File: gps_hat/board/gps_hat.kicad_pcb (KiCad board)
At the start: 2 copper layers, 12 parts, among them IC1 MTK3339, J1 Conn_02x10_Odd_Even, J2 U.FL-R-SMT(10)

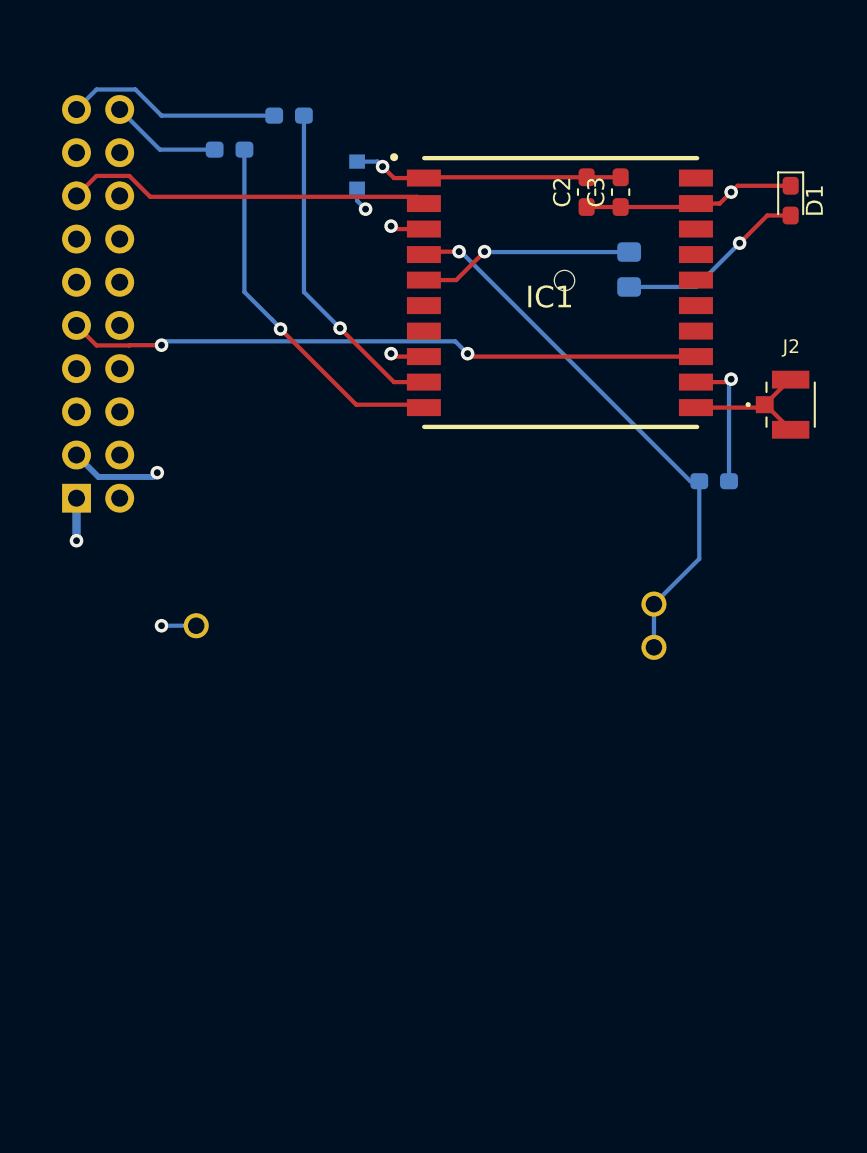
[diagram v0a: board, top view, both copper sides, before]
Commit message: Finished GPU_HAT
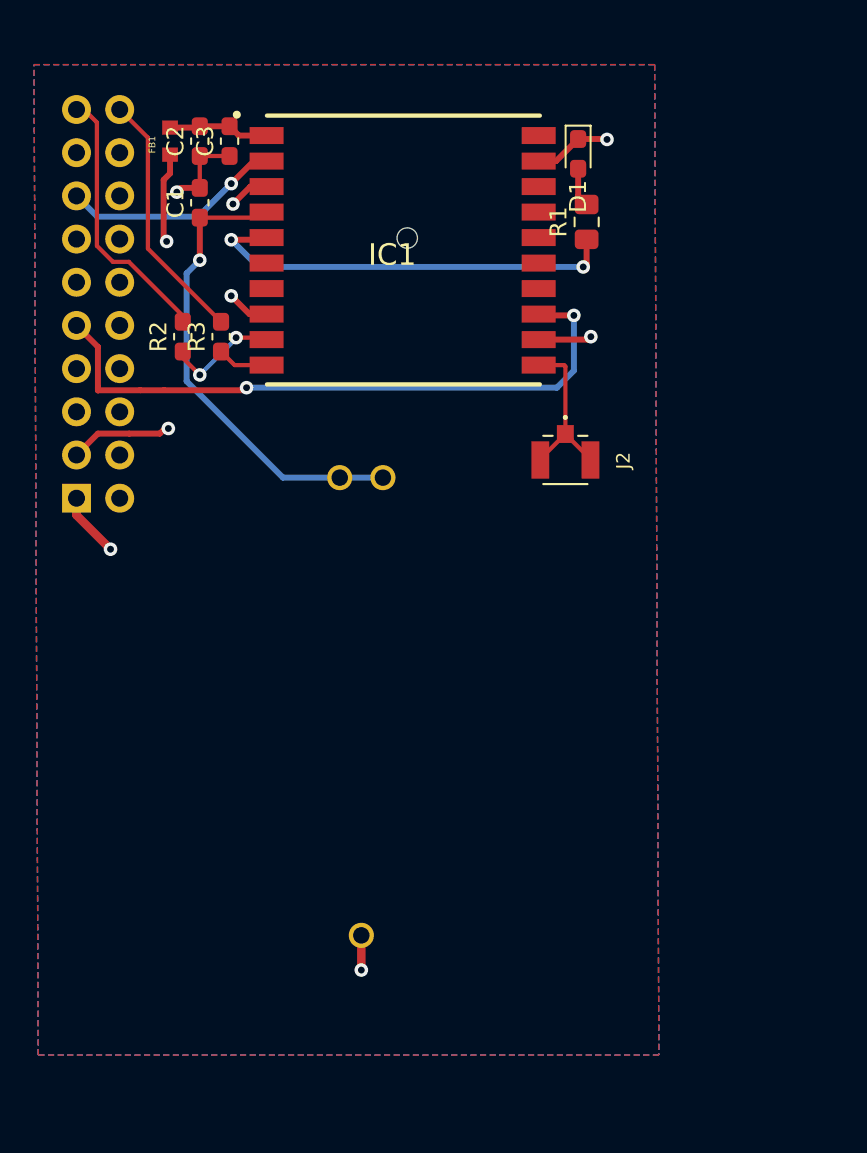
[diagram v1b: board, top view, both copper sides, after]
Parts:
- C1, FB1, R1, R2, R3: moved to F.Cu
- moved C1 34.4 mm to (136.2, 66.1), turned to 90 degrees
- moved C3 23.2 mm to (138.0, 62.5)
- moved C2 22.9 mm to (136.2, 62.5)
- moved R2 14.4 mm to (135.2, 74.0), turned to 90 degrees
- moved J2 13.6 mm to (157.8, 81.2), turned to 270 degrees
- moved D1 12.8 mm to (158.5, 63.2)
- moved FB1 11.2 mm to (134.5, 62.5)
- moved R3 11.0 mm to (137.5, 74.0), turned to 90 degrees
- moved IC1 9.58 mm to (156.2, 61.0)
- moved BT1 6.05 mm to (145.8, 95.8), turned to 270 degrees
- moved R1 3.75 mm to (159.0, 67.2), turned to 90 degrees
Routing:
- net Net-(IC1-Pad10): track 22.2 -> 3.47 mm, vias 1 -> 0
- net Net-(IC1-Pad9): track 19.6 -> 6.71 mm, vias 1 -> 2
- net Net-(IC1-Pad5): track 12.8 -> 25.2 mm, vias 1 -> 2
- net Net-(C2-Pad2): track 15.9 -> 5.94 mm, vias 1 -> 0
- net Net-(D1-Pad2): track 11.2 -> 2.31 mm, vias 1 -> 0
- net /NRESET: track 21.6 -> 13.0 mm, vias 0 -> 1
- net /TX: track 6.56 -> 15.0 mm
- net GND: track 29.3 -> 23.6 mm, vias 6 -> 7
- net Net-(BT1-Pad+1): track 32.7 -> 27.9 mm
- net +3V3: track 6.80 -> 11.4 mm
- net /RX: track 12.7 -> 15.9 mm
- net Net-(IC1-Pad11): track 8.39 -> 9.85 mm
- net /1PPS: track 37.4 -> 38.3 mm
- added copper zone on B.Cu, net +3V3
- added copper zone on B.Cu, net GND
- added copper zone on F.Cu, net GND

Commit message: Last Revision
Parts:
- added R1: MountingHole, MountingHole:MountingHole_3mm, F.Cu at (133.0, 60.0)
- added R2: MountingHole, MountingHole:MountingHole_3mm, F.Cu at (162.5, 60.0)
- moved BT1 7.38 mm to (149.2, 102.2)
- moved C1 7.38 mm to (139.8, 72.6)
- moved C2 7.38 mm to (139.8, 69.0)
- moved C3 7.38 mm to (141.5, 69.0)
- moved D1 7.38 mm to (162.0, 69.8)
- moved FB1 7.38 mm to (138.0, 69.0)
- moved IC1 7.38 mm to (159.8, 67.5)
- moved R1 7.16 mm to (162.0, 73.8)
- moved R2 6.90 mm to (140.0, 79.0)
- moved J2 6.38 mm to (160.5, 87.0)
- moved R3 5.52 mm to (138.0, 79.5)
- moved J1 5.42 mm to (131.5, 88.3)
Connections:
- J1 pad 19: /RX -> /TX
- J1 pad 20: /TX -> /RX
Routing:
- net +3V3: track 11.4 -> 20.0 mm, vias 2 -> 1
- net Net-(IC1-Pad10): track 3.47 -> 6.89 mm
- net Net-(IC1-Pad9): track 6.71 -> 4.01 mm, vias 2 -> 0
- net /TX: track 15.0 -> 16.9 mm
- net Net-(IC1-Pad11): track 9.85 -> 7.92 mm
- net GND: track 23.6 -> 22.8 mm
- net Net-(IC1-Pad5): track 25.2 -> 25.8 mm
- removed copper zone on B.Cu, net +3V3
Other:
- board outline added: 36.5 x 63.5 mm

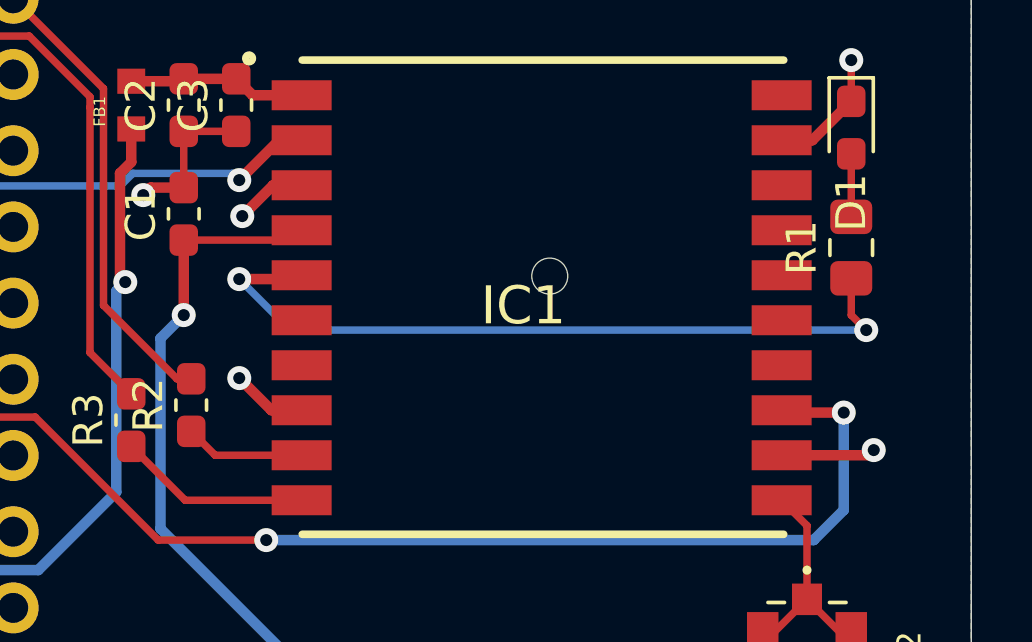
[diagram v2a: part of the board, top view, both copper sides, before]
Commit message: Fixed GPS GND
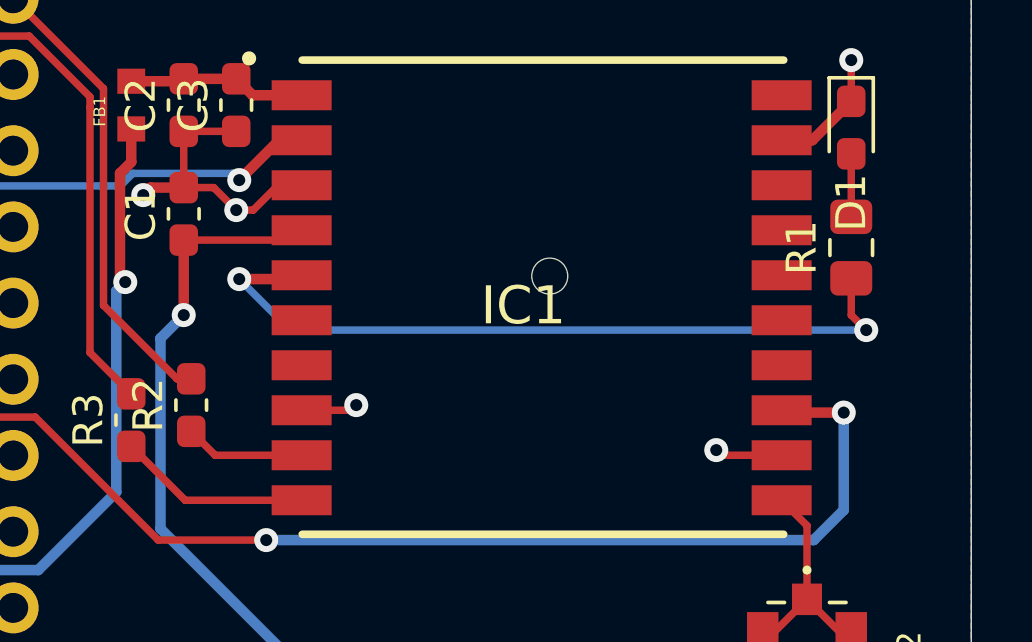
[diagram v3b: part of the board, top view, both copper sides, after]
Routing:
- net GND: track 22.8 -> 23.4 mm

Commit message: Fixed PCB Layout
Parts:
-  : renamed from R2
-  : renamed from R1
-  : renamed from BT1; moved to F.Cu
-  : renamed from J2
- moved R1 16.3 mm to (148.1, 65.4), turned to 0 degrees
- moved D1 10.9 mm to (152.1, 65.4), turned to 180 degrees
- moved   9.01 mm to (151.5, 87.4), turned to 180 degrees
- moved   5.20 mm to (144.2, 101.0), turned to 180 degrees
- moved R3 3.12 mm to (139.7, 82.2), turned to 180 degrees
- moved C3 2.24 mm to (139.6, 67.8), turned to 270 degrees
- moved C2 2.08 mm to (141.4, 67.8), turned to 270 degrees
- moved C1 1.68 mm to (141.4, 72.5)
- moved R2 1.37 mm to (139.7, 80.3), turned to 180 degrees
- moved FB1 0.47 mm to (137.8, 69.4)
- renumbered IC1 to GPS
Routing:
- net Net-(IC1-Pad5): track 25.8 -> 11.6 mm, vias 2 -> 0
- net /NRESET: track 13.5 -> 27.5 mm, vias 1 -> 0
- net Net-(BT1-Pad+1): track 27.9 -> 38.9 mm, vias 1 -> 2
- net GND: track 23.4 -> 16.8 mm, vias 7 -> 8
- net Net-(IC1-Pad11): track 7.92 -> 14.0 mm
- net /TX: track 16.9 -> 21.9 mm
- net Net-(IC1-Pad10): track 6.89 -> 3.16 mm
- net /1PPS: track 38.4 -> 41.7 mm, vias 2 -> 0
- net /RX: track 15.4 -> 18.0 mm
- net +3V3: track 20.0 -> 22.5 mm, vias 1 -> 0
- net Net-(IC1-Pad9): track 4.01 -> 3.30 mm
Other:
- board size 36.5 x 63.5 mm -> 37 x 55.1 mm

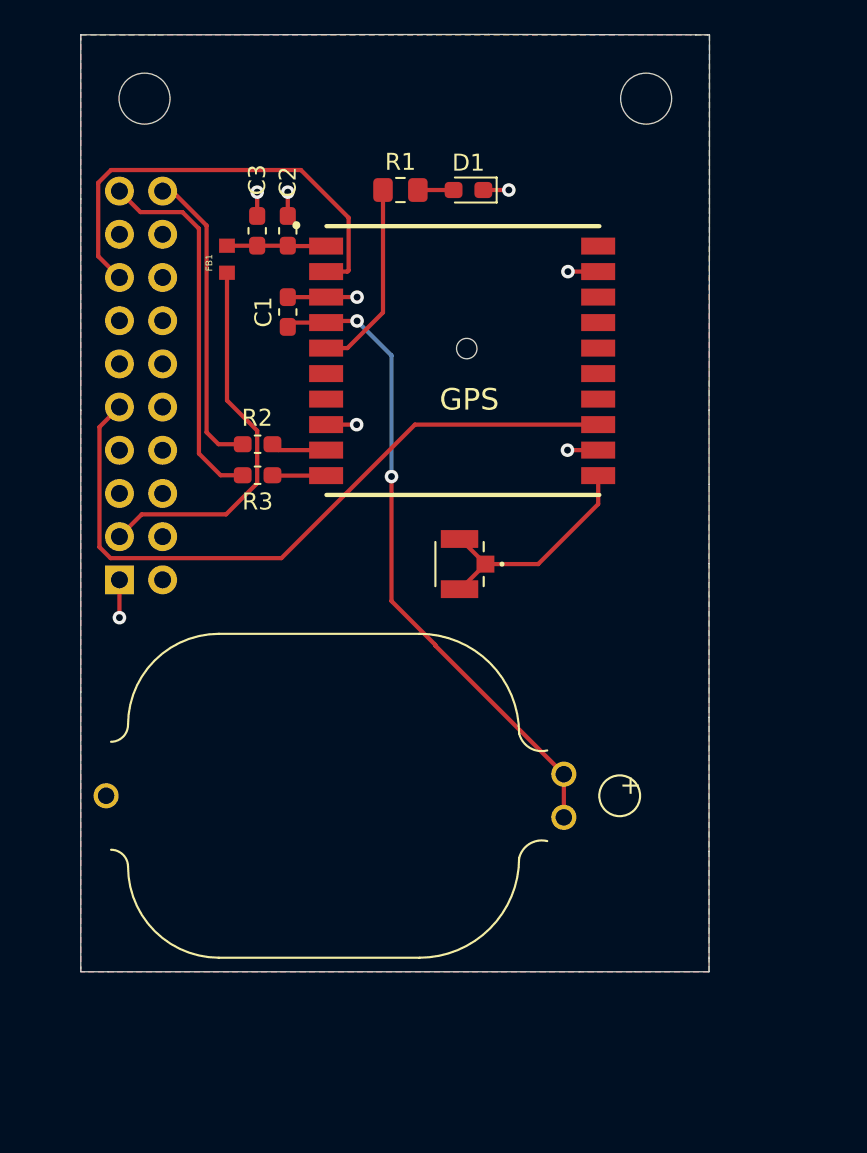
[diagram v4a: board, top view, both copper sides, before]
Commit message: Added Datasheets and Orderlinks
I also updated the U.FL connector so that it is closer and easier to solder onto the PCB
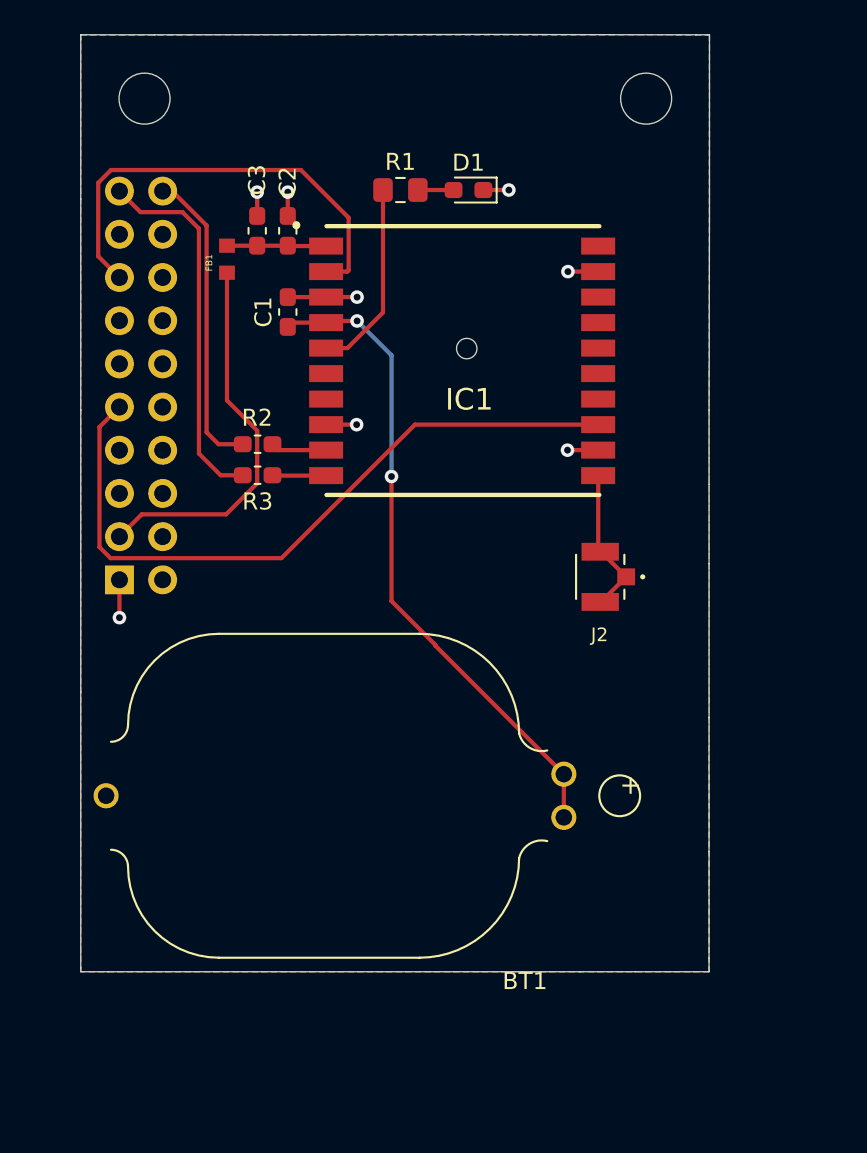
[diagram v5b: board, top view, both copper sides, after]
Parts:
- BT1, J2: renamed from  
- FB1: value FBMH1608HL601-T -> 600 Ohm
- moved J2 8.31 mm to (159.8, 88.1)
- renumbered GPS to IC1
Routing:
- net Net-(IC1-Pad11): track 14.0 -> 8.80 mm
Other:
- board text added: "HOLA"
